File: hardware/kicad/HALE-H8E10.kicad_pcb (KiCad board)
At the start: 2 copper layers, 0 parts

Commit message: WIP checkpoint commit before spliting the 5V rail
hardware/kicad/HALE-H8E10.kicad_pcb: Manufacturing: changed the board
  outline; tenting front back → -; covering - → -; plugging - → -;
  capping - → no; filling - → no; changed the plot output settings.
  Gergő Törcsvári: updated from the schematic (added C1003, C1004,
  C2001-C2016, C3001, C3002, C21001 and 83 more, TP1001-TP1003 not
  placed yet); placed C1003, C1004, C2001-C2016, C3001, C3002, C21001
  and 82 more; routed D_CS, DS_BL, DS_RES, E_INT and 86 more nets; added
  a zone on F.Cu, B.Cu; added a zone on F.Cu, B.Cu; added a zone on
  F.Cu, B.Cu; added a zone on F.Cu, B.Cu; and 15 more changes.
hardware/kicad/HALE-H8E10.kicad_pro: Manufacturing: max arc error - →
  0.005 mm; min connection width - → 0 mm; min groove width - → 0 mm;
  min microvia diameter - → 0.2 mm; min microvia drill - → 0.1 mm; min
  resolved spokes - → 2 mm; solder mask to copper clearance - → 0 mm;
  use height for length calcs - → true mm. Gergő Törcsvári: changed the
  predefined track widths (+4); changed the predefined diff pair sizes
  (+1); changed teardrop settings; changed default text and line
  settings; changed 62 DRC rule severities; changed DRC exclusions;
  changed schematic settings; changed 19 board.design settings settings.
hardware/kicad/HALE-H8E10.kicad_sch: Gergő Törcsvári added R1002, R1003
  and TP1001-TP1003 and wired them; removed C1001, C1002, C1005, D1001
  and D1002; changed C1004 value 100nF → 10uF; changed C1004 footprint
  Capacitor_SMD:C_0603_1608Metric_Pad1.08x0.95mm_HandSolder →
  Capacitor_SMD:C_0805_2012Metric_Pad1.18x1.45mm_HandSolder; changed
  C1004 LCSC C14663 → C15850; changed C1004 wiring (pins 1 and 2 now on
  GND and +5V); changed DS1001 wiring (pin 7 now on /D_CS); and 4 more
  changes.
hardware/kicad/encoders.kicad_sch: Gergő Törcsvári changed U3001 wiring;
  changed U3002 wiring; rearranged the sheet.
hardware/kicad/keys.kicad_sch: Gergő Törcsvári added TP2001 (3V3A) and
  wired it; change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
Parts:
- added C1003: 100nF, Capacitor_SMD:C_0603_1608Metric_Pad1.08x0.95mm_HandSolder, B.Cu at (97.5, 67.5)
- added C1004: 10uF, Capacitor_SMD:C_0805_2012Metric_Pad1.18x1.45mm_HandSolder, B.Cu at (113.5, 107.0)
- added C2001: 10uF, Capacitor_SMD:C_0805_2012Metric_Pad1.18x1.45mm_HandSolder, B.Cu at (55.6, 69.8)
- added C2002: 10uF, Capacitor_SMD:C_0805_2012Metric_Pad1.18x1.45mm_HandSolder, B.Cu at (46.1, 67.5)
- added C2003: 100nF, Capacitor_SMD:C_0603_1608Metric_Pad1.08x0.95mm_HandSolder, B.Cu at (47.9, 67.8)
- added C2004: 100nF, Capacitor_SMD:C_0603_1608Metric_Pad1.08x0.95mm_HandSolder, B.Cu at (44.1, 85.6)
- added C2005: 100nF, Capacitor_SMD:C_0603_1608Metric_Pad1.08x0.95mm_HandSolder, B.Cu at (42.6, 85.6)
- added C2006: 10uF, Capacitor_SMD:C_0805_2012Metric_Pad1.18x1.45mm_HandSolder, B.Cu at (43.2, 72.5)
- added C2007: 100nF, Capacitor_SMD:C_0603_1608Metric_Pad1.08x0.95mm_HandSolder, B.Cu at (45.8, 85.6)
- added C2008: 100nF, Capacitor_SMD:C_0603_1608Metric_Pad1.08x0.95mm_HandSolder, B.Cu at (40.8, 85.6)
- added C2009: 100nF, Capacitor_SMD:C_0603_1608Metric_Pad1.08x0.95mm_HandSolder, B.Cu at (43.5, 74.2)
- added C2010: 100nF, Capacitor_SMD:C_0603_1608Metric_Pad1.08x0.95mm_HandSolder, B.Cu at (47.6, 85.6)
- added C2011: 100nF, Capacitor_SMD:C_0603_1608Metric_Pad1.08x0.95mm_HandSolder, B.Cu at (39.1, 85.6)
- added C2012: 100nF, Capacitor_SMD:C_0603_1608Metric_Pad1.08x0.95mm_HandSolder, B.Cu at (49.3, 85.6)
- added C2013: 100nF, Capacitor_SMD:C_0603_1608Metric_Pad1.08x0.95mm_HandSolder, B.Cu at (37.3, 85.6)
- added C2014: 100nF, Capacitor_SMD:C_0603_1608Metric_Pad1.08x0.95mm_HandSolder, B.Cu at (47.6, 74.6)
- added C2015: 100nF, Capacitor_SMD:C_0603_1608Metric_Pad1.08x0.95mm_HandSolder, B.Cu at (46.1, 74.6)
- added C2016: 1uF, Capacitor_SMD:C_0603_1608Metric_Pad1.08x0.95mm_HandSolder, B.Cu at (49.1, 74.6)
- added C21001: 100nF, Capacitor_SMD:C_0603_1608Metric_Pad1.08x0.95mm_HandSolder, B.Cu at (42.9, 109.3)
- added C21002: 100nF, Capacitor_SMD:C_0603_1608Metric_Pad1.08x0.95mm_HandSolder, B.Cu at (36.4, 99.7)
- added C22001: 100nF, Capacitor_SMD:C_0603_1608Metric_Pad1.08x0.95mm_HandSolder, B.Cu at (61.9, 109.3)
- added C22002: 100nF, Capacitor_SMD:C_0603_1608Metric_Pad1.08x0.95mm_HandSolder, B.Cu at (55.5, 99.7)
- added C23001: 100nF, Capacitor_SMD:C_0603_1608Metric_Pad1.08x0.95mm_HandSolder, B.Cu at (81.0, 109.3)
- added C23002: 100nF, Capacitor_SMD:C_0603_1608Metric_Pad1.08x0.95mm_HandSolder, B.Cu at (74.5, 99.7)
- added C24001: 100nF, Capacitor_SMD:C_0603_1608Metric_Pad1.08x0.95mm_HandSolder, B.Cu at (100.0, 109.3)
- added C24002: 100nF, Capacitor_SMD:C_0603_1608Metric_Pad1.08x0.95mm_HandSolder, B.Cu at (93.5, 99.7)
- added C25001: 100nF, Capacitor_SMD:C_0603_1608Metric_Pad1.08x0.95mm_HandSolder, B.Cu at (42.9, 128.3)
- added C25002: 100nF, Capacitor_SMD:C_0603_1608Metric_Pad1.08x0.95mm_HandSolder, B.Cu at (36.4, 118.7)
- added C26001: 100nF, Capacitor_SMD:C_0603_1608Metric_Pad1.08x0.95mm_HandSolder, B.Cu at (61.9, 128.3)
- added C26002: 100nF, Capacitor_SMD:C_0603_1608Metric_Pad1.08x0.95mm_HandSolder, B.Cu at (55.5, 118.7)
- added C27001: 100nF, Capacitor_SMD:C_0603_1608Metric_Pad1.08x0.95mm_HandSolder, B.Cu at (81.0, 128.3)
- added C27002: 100nF, Capacitor_SMD:C_0603_1608Metric_Pad1.08x0.95mm_HandSolder, B.Cu at (74.5, 118.7)
- added C28001: 100nF, Capacitor_SMD:C_0603_1608Metric_Pad1.08x0.95mm_HandSolder, B.Cu at (100.0, 128.3)
- added C28002: 100nF, Capacitor_SMD:C_0603_1608Metric_Pad1.08x0.95mm_HandSolder, B.Cu at (93.5, 118.7)
- added C3001: 100nF, Capacitor_SMD:C_0603_1608Metric_Pad1.08x0.95mm_HandSolder, B.Cu at (151.5, 107.2)
- added C3002: 100nF, Capacitor_SMD:C_0603_1608Metric_Pad1.08x0.95mm_HandSolder, B.Cu at (214.0, 107.2)
- added C31001: 1nF, Capacitor_SMD:C_0603_1608Metric_Pad1.08x0.95mm_HandSolder, B.Cu at (129.0, 70.3)
- added C31002: 1nF, Capacitor_SMD:C_0603_1608Metric_Pad1.08x0.95mm_HandSolder, B.Cu at (119.0, 70.3)
- added C31003: 100nF, Capacitor_SMD:C_0603_1608Metric_Pad1.08x0.95mm_HandSolder, B.Cu at (128.5, 89.0)
- added C32001: 1nF, Capacitor_SMD:C_0603_1608Metric_Pad1.08x0.95mm_HandSolder, B.Cu at (156.0, 70.3)
- added C32002: 1nF, Capacitor_SMD:C_0603_1608Metric_Pad1.08x0.95mm_HandSolder, B.Cu at (146.0, 70.3)
- added C32003: 100nF, Capacitor_SMD:C_0603_1608Metric_Pad1.08x0.95mm_HandSolder, B.Cu at (155.5, 89.0)
- added C33001: 1nF, Capacitor_SMD:C_0603_1608Metric_Pad1.08x0.95mm_HandSolder, B.Cu at (183.0, 70.3)
- added C33002: 1nF, Capacitor_SMD:C_0603_1608Metric_Pad1.08x0.95mm_HandSolder, B.Cu at (173.0, 70.3)
- added C33003: 100nF, Capacitor_SMD:C_0603_1608Metric_Pad1.08x0.95mm_HandSolder, B.Cu at (182.5, 89.0)
- added C34001: 1nF, Capacitor_SMD:C_0603_1608Metric_Pad1.08x0.95mm_HandSolder, B.Cu at (210.0, 70.3)
- added C34002: 1nF, Capacitor_SMD:C_0603_1608Metric_Pad1.08x0.95mm_HandSolder, B.Cu at (200.0, 70.3)
- added C34003: 100nF, Capacitor_SMD:C_0603_1608Metric_Pad1.08x0.95mm_HandSolder, B.Cu at (209.5, 89.0)
- added C35001: 1nF, Capacitor_SMD:C_0603_1608Metric_Pad1.08x0.95mm_HandSolder, B.Cu at (237.0, 70.3)
- added C35002: 1nF, Capacitor_SMD:C_0603_1608Metric_Pad1.08x0.95mm_HandSolder, B.Cu at (227.0, 70.3)
- added C35003: 100nF, Capacitor_SMD:C_0603_1608Metric_Pad1.08x0.95mm_HandSolder, B.Cu at (236.5, 89.0)
- added C36001: 1nF, Capacitor_SMD:C_0603_1608Metric_Pad1.08x0.95mm_HandSolder, B.Cu at (119.0, 131.8)
- added C36002: 1nF, Capacitor_SMD:C_0603_1608Metric_Pad1.08x0.95mm_HandSolder, B.Cu at (129.0, 131.8)
- added C36003: 100nF, Capacitor_SMD:C_0603_1608Metric_Pad1.08x0.95mm_HandSolder, B.Cu at (119.5, 113.1)
- added C37001: 1nF, Capacitor_SMD:C_0603_1608Metric_Pad1.08x0.95mm_HandSolder, B.Cu at (146.0, 131.8)
- added C37002: 1nF, Capacitor_SMD:C_0603_1608Metric_Pad1.08x0.95mm_HandSolder, B.Cu at (156.0, 131.8)
- added C37003: 100nF, Capacitor_SMD:C_0603_1608Metric_Pad1.08x0.95mm_HandSolder, B.Cu at (146.5, 113.1)
- added C38001: 1nF, Capacitor_SMD:C_0603_1608Metric_Pad1.08x0.95mm_HandSolder, B.Cu at (173.0, 131.8)
- added C38002: 1nF, Capacitor_SMD:C_0603_1608Metric_Pad1.08x0.95mm_HandSolder, B.Cu at (183.0, 131.8)
- added C38003: 100nF, Capacitor_SMD:C_0603_1608Metric_Pad1.08x0.95mm_HandSolder, B.Cu at (173.5, 113.1)
- added C39001: 1nF, Capacitor_SMD:C_0603_1608Metric_Pad1.08x0.95mm_HandSolder, B.Cu at (200.0, 131.8)
- added C39002: 1nF, Capacitor_SMD:C_0603_1608Metric_Pad1.08x0.95mm_HandSolder, B.Cu at (210.0, 131.8)
- added C39003: 100nF, Capacitor_SMD:C_0603_1608Metric_Pad1.08x0.95mm_HandSolder, B.Cu at (200.5, 113.1)
- added C40001: 1nF, Capacitor_SMD:C_0603_1608Metric_Pad1.08x0.95mm_HandSolder, B.Cu at (227.0, 131.8)
- added C40002: 1nF, Capacitor_SMD:C_0603_1608Metric_Pad1.08x0.95mm_HandSolder, B.Cu at (237.0, 131.8)
- added C40003: 100nF, Capacitor_SMD:C_0603_1608Metric_Pad1.08x0.95mm_HandSolder, B.Cu at (227.5, 113.1)
- added D21001: SK6812MINI-E, LED_SMD:LED_SK6812MINI-E_3.2x2.8mm_P1.5mm_ReverseMount, B.Cu at (41.0, 101.4)
- added D22001: SK6812MINI-E, LED_SMD:LED_SK6812MINI-E_3.2x2.8mm_P1.5mm_ReverseMount, B.Cu at (60.0, 101.4)
- added D23001: SK6812MINI-E, LED_SMD:LED_SK6812MINI-E_3.2x2.8mm_P1.5mm_ReverseMount, B.Cu at (79.0, 101.4)
- added D24001: SK6812MINI-E, LED_SMD:LED_SK6812MINI-E_3.2x2.8mm_P1.5mm_ReverseMount, B.Cu at (98.1, 101.4)
- added D25001: SK6812MINI-E, LED_SMD:LED_SK6812MINI-E_3.2x2.8mm_P1.5mm_ReverseMount, B.Cu at (41.0, 120.5)
- added D26001: SK6812MINI-E, LED_SMD:LED_SK6812MINI-E_3.2x2.8mm_P1.5mm_ReverseMount, B.Cu at (60.0, 120.5)
- added D27001: SK6812MINI-E, LED_SMD:LED_SK6812MINI-E_3.2x2.8mm_P1.5mm_ReverseMount, B.Cu at (79.0, 120.5)
- added D28001: SK6812MINI-E, LED_SMD:LED_SK6812MINI-E_3.2x2.8mm_P1.5mm_ReverseMount, B.Cu at (98.1, 120.5)
- added D31001: SK6812MINI-E, LED_SMD:LED_SK6812MINI-E_3.2x2.8mm_P1.5mm_ReverseMount, B.Cu at (124.0, 87.3)
- added D32001: SK6812MINI-E, LED_SMD:LED_SK6812MINI-E_3.2x2.8mm_P1.5mm_ReverseMount, B.Cu at (151.0, 87.3)
- added D33001: SK6812MINI-E, LED_SMD:LED_SK6812MINI-E_3.2x2.8mm_P1.5mm_ReverseMount, B.Cu at (178.0, 87.3)
- added D34001: SK6812MINI-E, LED_SMD:LED_SK6812MINI-E_3.2x2.8mm_P1.5mm_ReverseMount, B.Cu at (205.0, 87.3)
- added D35001: SK6812MINI-E, LED_SMD:LED_SK6812MINI-E_3.2x2.8mm_P1.5mm_ReverseMount, B.Cu at (232.0, 87.3)
- added D36001: SK6812MINI-E, LED_SMD:LED_SK6812MINI-E_3.2x2.8mm_P1.5mm_ReverseMount, B.Cu at (124.0, 114.8)
- added D37001: SK6812MINI-E, LED_SMD:LED_SK6812MINI-E_3.2x2.8mm_P1.5mm_ReverseMount, B.Cu at (151.0, 114.8)
- added D38001: SK6812MINI-E, LED_SMD:LED_SK6812MINI-E_3.2x2.8mm_P1.5mm_ReverseMount, B.Cu at (178.0, 114.8)
- added D39001: SK6812MINI-E, LED_SMD:LED_SK6812MINI-E_3.2x2.8mm_P1.5mm_ReverseMount, B.Cu at (205.0, 114.8)
- added D40001: SK6812MINI-E, LED_SMD:LED_SK6812MINI-E_3.2x2.8mm_P1.5mm_ReverseMount, B.Cu at (232.0, 114.8)
- added DS1001: Screen, HALE-git:Display_2.79_NV3007, F.Cu at (69.5, 76.8)
- added FB2001: FerriteBead, Inductor_SMD:L_0603_1608Metric_Pad1.05x0.95mm_HandSolder, B.Cu at (44.2, 69.8)
- added K21001: ks-20, HALE-git:Gateron_KS-20, F.Cu at (40.9, 106.3)
- added K22001: ks-20, HALE-git:Gateron_KS-20, F.Cu at (60.0, 106.3)
- added K23001: ks-20, HALE-git:Gateron_KS-20, F.Cu at (79.0, 106.3)
- added K24001: ks-20, HALE-git:Gateron_KS-20, F.Cu at (98.1, 106.3)
- added K25001: ks-20, HALE-git:Gateron_KS-20, F.Cu at (40.9, 125.3)
- added K26001: ks-20, HALE-git:Gateron_KS-20, F.Cu at (60.0, 125.3)
- added K27001: ks-20, HALE-git:Gateron_KS-20, F.Cu at (79.0, 125.3)
- added K28001: ks-20, HALE-git:Gateron_KS-20, F.Cu at (98.1, 125.3)
- added R1001: 220, Resistor_SMD:R_0603_1608Metric_Pad0.98x0.95mm_HandSolder, B.Cu at (98.5, 64.5)
- added R1002: 10K, Resistor_SMD:R_0603_1608Metric_Pad0.98x0.95mm_HandSolder, B.Cu at (88.2, 66.8)
- added R1003: 10K, Resistor_SMD:R_0603_1608Metric_Pad0.98x0.95mm_HandSolder, B.Cu at (69.2, 83.8)
- added R3001: 4.7K, Resistor_SMD:R_0603_1608Metric_Pad0.98x0.95mm_HandSolder, B.Cu at (88.2, 76.8)
- added R3002: 4.7K, Resistor_SMD:R_0603_1608Metric_Pad0.98x0.95mm_HandSolder, B.Cu at (88.2, 74.5)
- added R3003: 10K, Resistor_SMD:R_0603_1608Metric_Pad0.98x0.95mm_HandSolder, B.Cu at (88.2, 72.0)
- added R3004: 10K, Resistor_SMD:R_0603_1608Metric_Pad0.98x0.95mm_HandSolder, B.Cu at (90.2, 79.2)
- added RN2001: 1k, Resistor_SMD:R_Array_Convex_4x0603, B.Cu at (48.1, 90.8)
- added RN2002: 1k, Resistor_SMD:R_Array_Convex_4x0603, B.Cu at (38.6, 91.1)
- added SW31001: RotaryEncoder_Switch_MP, HALE-git:RotaryEncoder_Alps_EC12E-Switch_Vertical_H20mm, F.Cu at (124.0, 76.8)
- added SW32001: RotaryEncoder_Switch_MP, HALE-git:RotaryEncoder_Alps_EC12E-Switch_Vertical_H20mm, F.Cu at (151.0, 76.8)
- added SW33001: RotaryEncoder_Switch_MP, HALE-git:RotaryEncoder_Alps_EC12E-Switch_Vertical_H20mm, F.Cu at (178.0, 76.8)
- added SW34001: RotaryEncoder_Switch_MP, HALE-git:RotaryEncoder_Alps_EC12E-Switch_Vertical_H20mm, F.Cu at (205.0, 76.8)
- added SW35001: RotaryEncoder_Switch_MP, HALE-git:RotaryEncoder_Alps_EC12E-Switch_Vertical_H20mm, F.Cu at (232.0, 76.8)
- added SW36001: RotaryEncoder_Switch_MP, HALE-git:RotaryEncoder_Alps_EC12E-Switch_Vertical_H20mm, F.Cu at (124.0, 125.3)
- added SW37001: RotaryEncoder_Switch_MP, HALE-git:RotaryEncoder_Alps_EC12E-Switch_Vertical_H20mm, F.Cu at (151.0, 125.3)
- added SW38001: RotaryEncoder_Switch_MP, HALE-git:RotaryEncoder_Alps_EC12E-Switch_Vertical_H20mm, F.Cu at (178.0, 125.3)
- added SW39001: RotaryEncoder_Switch_MP, HALE-git:RotaryEncoder_Alps_EC12E-Switch_Vertical_H20mm, F.Cu at (205.0, 125.3)
- added SW40001: RotaryEncoder_Switch_MP, HALE-git:RotaryEncoder_Alps_EC12E-Switch_Vertical_H20mm, F.Cu at (232.0, 125.3)
- added TP1001: 5V, TestPoint:TestPoint_Pad_D2.0mm, B.Cu at (46.2, 41.8)
- added TP1002: GND, TestPoint:TestPoint_Pad_D2.0mm, B.Cu at (46.2, 45.9)
- added TP1003: 3V3, TestPoint:TestPoint_Pad_D2.0mm, B.Cu at (46.2, 49.9)
- added TP2001: 3V3A, TestPoint:TestPoint_Pad_D2.0mm, B.Cu at (38.5, 70.8)
- added U1001: 74AHCT1G125, Package_TO_SOT_SMD:SOT-23-5, B.Cu at (94.5, 65.2)
- added U1002: XIAO-ESP32-S3-Plus-SMD, HALE-git:XIAO-ESP32-S3-Plus-SMD, B.Cu at (75.0, 71.8)
- added U2001: ME6211C33M5, Package_TO_SOT_SMD:SOT-23-5, B.Cu at (50.9, 69.8)
- added U2002: MCP3208, Package_SO:SOIC-16_3.9x9.9mm_P1.27mm, B.Cu at (43.1, 80.1)
- added U21001: DRV5055A3xDBZxQ1, Package_TO_SOT_SMD:SOT-23, B.Cu at (41.0, 106.3)
- added U22001: DRV5055A3xDBZxQ1, Package_TO_SOT_SMD:SOT-23, B.Cu at (60.0, 106.3)
- added U23001: DRV5055A3xDBZxQ1, Package_TO_SOT_SMD:SOT-23, B.Cu at (79.0, 106.3)
- added U24001: DRV5055A3xDBZxQ1, Package_TO_SOT_SMD:SOT-23, B.Cu at (98.1, 106.3)
- added U25001: DRV5055A3xDBZxQ1, Package_TO_SOT_SMD:SOT-23, B.Cu at (41.0, 125.3)
- added U26001: DRV5055A3xDBZxQ1, Package_TO_SOT_SMD:SOT-23, B.Cu at (60.0, 125.3)
- added U27001: DRV5055A3xDBZxQ1, Package_TO_SOT_SMD:SOT-23, B.Cu at (79.0, 125.3)
- added U28001: DRV5055A3xDBZxQ1, Package_TO_SOT_SMD:SOT-23, B.Cu at (98.1, 125.3)
- added U3001: MCP23017x-x-SS, Package_SO:SSOP-28_5.3x10.2mm_P0.65mm, B.Cu at (153.8, 101.8)
- added U3002: MCP23017x-x-SS, Package_SO:SSOP-28_5.3x10.2mm_P0.65mm, B.Cu at (216.0, 101.8)
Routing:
- net +5V: track 0.00 -> 653.2 mm, vias 0 -> 30
- net +3.3V: track 0.00 -> 195.5 mm, vias 0 -> 8
- net /encoders/I2C_SDA: track 0.00 -> 148.3 mm, vias 0 -> 2
- net /E_INT: track 0.00 -> 141.5 mm, vias 0 -> 3
- net /encoders/I2C_SCL: track 0.00 -> 130.5 mm, vias 0 -> 2
- net /encoders/RESET: track 0.00 -> 117.9 mm, vias 0 -> 2
- net /keys/H4: track 0.00 -> 106.8 mm
- net /keys/LED_L1_OUT: track 0.00 -> 106.4 mm, vias 0 -> 3
- net /keys/H8: track 0.00 -> 105.7 mm
- net GND: track 0.00 -> 97.8 mm, vias 0 -> 47
- net /keys/H3: track 0.00 -> 87.2 mm
- net /keys/H7: track 0.00 -> 85.2 mm
- net /encoders/ENC_B6: track 0.00 -> 81.9 mm
- net /encoders/ENC_B3: track 0.00 -> 74.0 mm
- net /E6_SW: track 0.00 -> 71.2 mm, vias 0 -> 2
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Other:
- board outline added: 217 x 77.7 mm

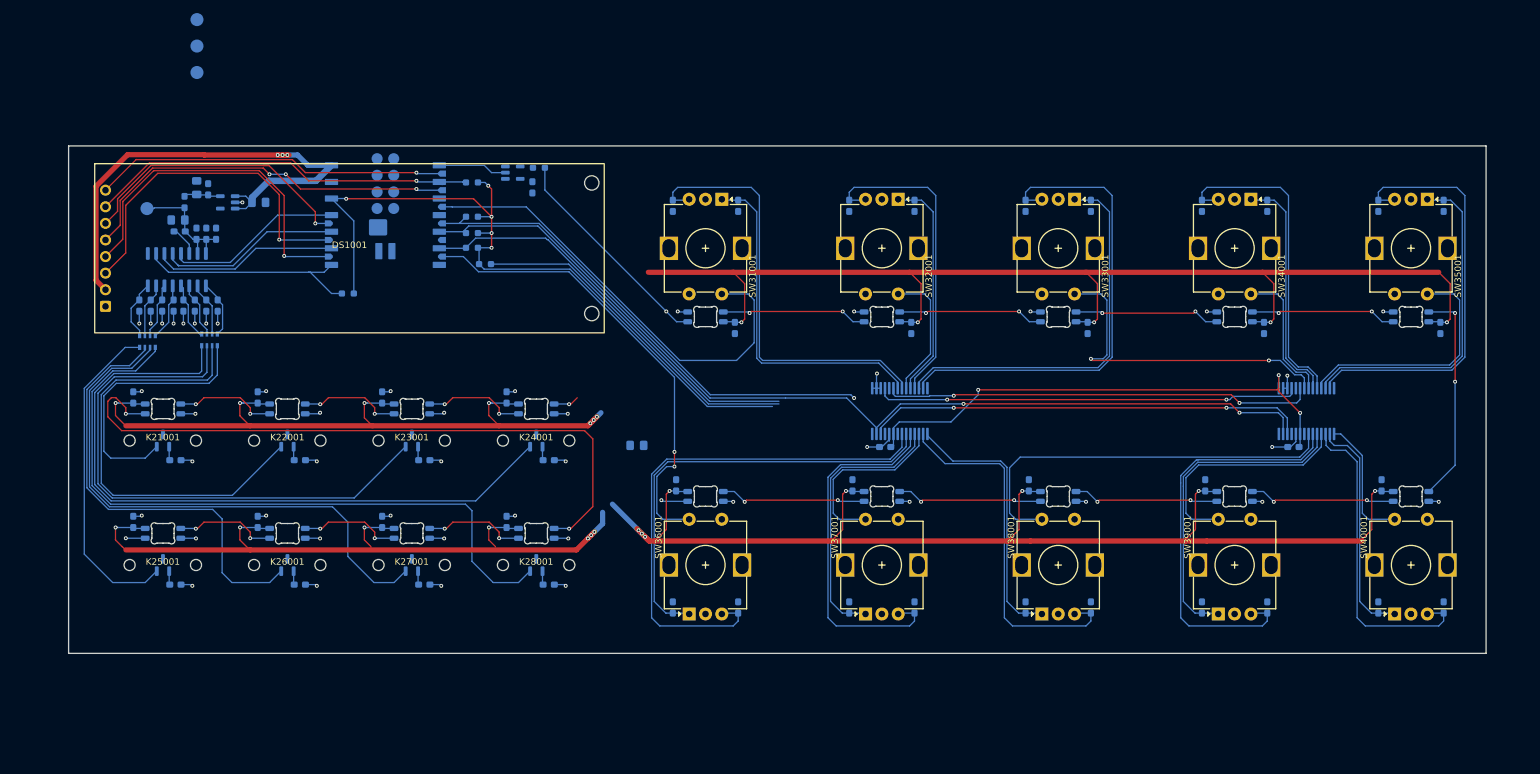
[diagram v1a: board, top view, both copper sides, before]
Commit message: "finished" PCB
hardware/kicad/HALE-H8E10.kicad_pcb: Manufacturing: changed the board
  outline. Gergő Törcsvári: updated from the schematic (added C1001,
  C1002, C1004-C1009, H1001-H1012, R1004, R1005 and 5 more; removed
  R1002 and R1003; nets changed on 44 pads); placed C1001, C1002,
  C1004-C1009, H1001-H1012, R1004, R1005 and 4 more; added REF**;
  removed C1004; moved C1003, C2002, C2003, C2006, R1001, TP2001 and
  U1001; routed EN_AUX, EN_LED, +5V_AUX, +5V_LED and 3 more nets;
  rerouted D_CS, DS_BL, DS_RES, E_INT and 21 more nets; and 3 more
  changes.
hardware/kicad/HALE-H8E10.kicad_pro: Gergő Törcsvári excluded 2 DRC
  violations; changed schematic settings.
hardware/kicad/HALE-H8E10.kicad_sch: Gergő Törcsvári added C1001, C1002,
  C1005-C1009, H1001-H1012, R1004, R1005 and 4 more and wired them;
  removed R1002 and R1003; changed 4 parts' fields; changed C1004 wiring
  (pin 1 now on +5V); renamed net unconnected-(U1002-D3-Pad4) to
  /EN_AUX; renamed net unconnected-(U1002-D15-Pad19) to /EN_LED; split
  +5V into +5V_AUX and +5V_LED; and 4 more changes.
hardware/kicad/encoder.kicad_sch: Gergő Törcsvári changed 10 parts'
  fields; renamed net unconnected-(U1002-D3-Pad4) to /EN_AUX; renamed
  net unconnected-(U1002-D15-Pad19) to /EN_LED; split +5V into +5V_AUX
  and +5V_LED.
hardware/kicad/encoders.kicad_sch: Gergő Törcsvári changed 6 parts'
  fields; renamed net unconnected-(U1002-D3-Pad4) to /EN_AUX; renamed
  net unconnected-(U1002-D15-Pad19) to /EN_LED; split +5V into +5V_AUX
  and +5V_LED.
hardware/kicad/key_cell.kicad_sch: Gergő Törcsvári changed 16 parts'
  fields; renamed net unconnected-(U1002-D3-Pad4) to /EN_AUX; renamed
  net unconnected-(U1002-D15-Pad19) to /EN_LED; split +5V into +5V_AUX
  and +5V_LED.
hardware/kicad/keys.kicad_sch: Gergő Törcsvári added R2001 (10K) and
  wired it to /KEYS_CS; changed 6 parts' fields; renamed net
  unconnected-(U1002-D3-Pad4) to /EN_AUX; renamed net
  unconnected-(U1002-D15-Pad19) to /EN_LED; split +5V into +5V_A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
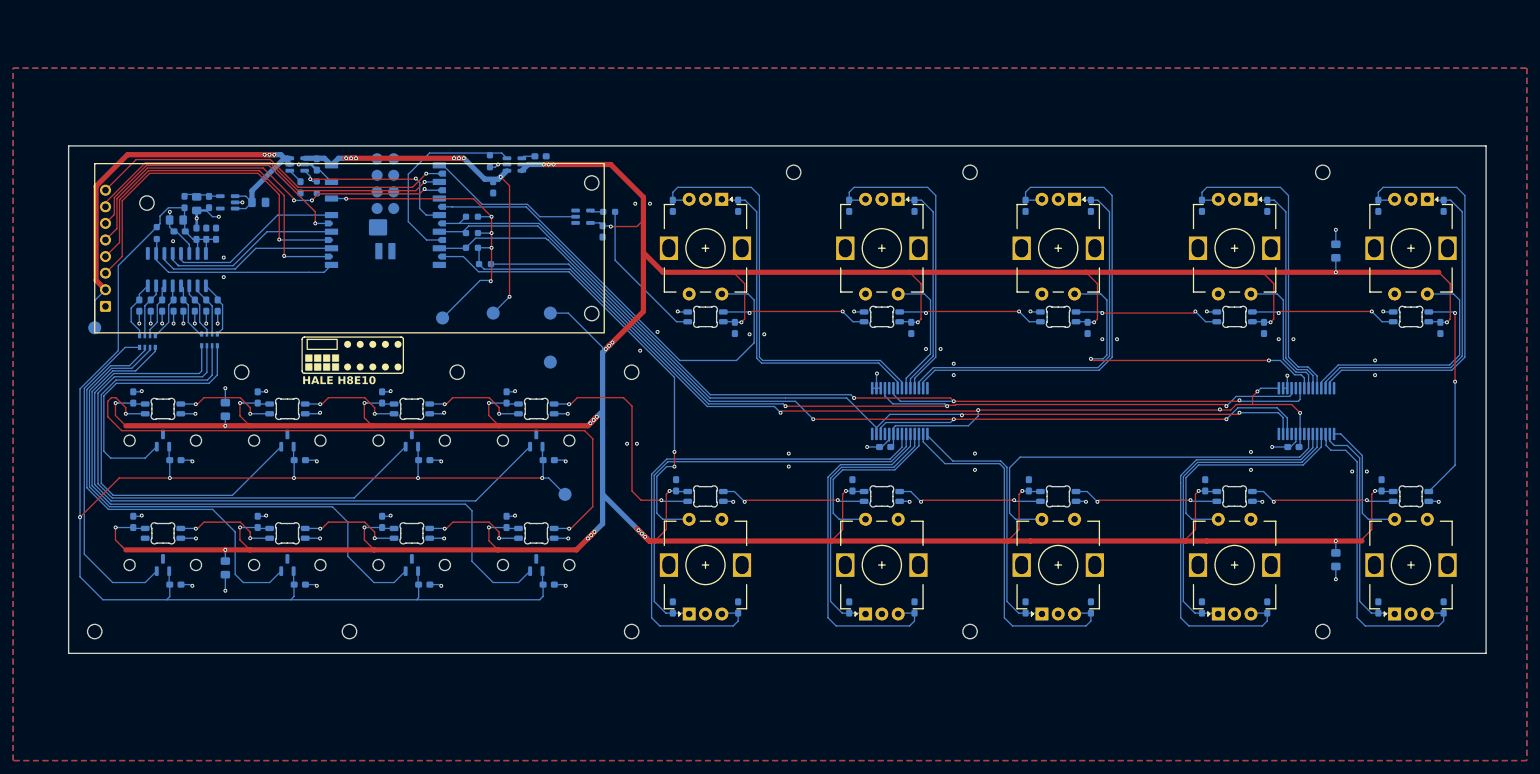
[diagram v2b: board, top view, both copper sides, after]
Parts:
- removed R1002, R1003: 10K, Resistor_SMD:R_0603_1608Metric_Pad0.98x0.95mm_HandSolder
- added C1001: 100nF, Capacitor_SMD:C_0603_1608Metric_Pad1.08x0.95mm_HandSolder, B.Cu at (62.0, 67.5)
- added C1002: 100nF, Capacitor_SMD:C_0603_1608Metric_Pad1.08x0.95mm_HandSolder, B.Cu at (98.8, 62.8)
- added C1005: 1uF, Capacitor_SMD:C_0603_1608Metric_Pad1.08x0.95mm_HandSolder, B.Cu at (64.5, 64.0)
- added C1006: 10uF, Capacitor_SMD:C_0805_2012Metric_Pad1.18x1.45mm_HandSolder, B.Cu at (50.5, 101.5)
- added C1007: 10uF, Capacitor_SMD:C_0805_2012Metric_Pad1.18x1.45mm_HandSolder, B.Cu at (50.5, 125.8)
- added C1008: 10uF, Capacitor_SMD:C_0805_2012Metric_Pad1.18x1.45mm_HandSolder, B.Cu at (220.5, 77.2)
- added C1009: 10uF, Capacitor_SMD:C_0805_2012Metric_Pad1.18x1.45mm_HandSolder, B.Cu at (220.5, 124.5)
- added H1001: MountingHole, MountingHole:MountingHole_2.2mm_M2, F.Cu at (30.5, 135.5)
- added H1002: MountingHole, MountingHole:MountingHole_2.2mm_M2, F.Cu at (69.5, 135.5)
- added H1003: MountingHole, MountingHole:MountingHole_2.2mm_M2, F.Cu at (112.7, 135.5)
- added H1004: MountingHole, MountingHole:MountingHole_2.2mm_M2, F.Cu at (53.0, 95.8)
- added H1005: MountingHole, MountingHole:MountingHole_2.2mm_M2, F.Cu at (86.0, 95.8)
- added H1006: MountingHole, MountingHole:MountingHole_2.2mm_M2, F.Cu at (112.7, 95.8)
- added H1007: MountingHole, MountingHole:MountingHole_2.2mm_M2, F.Cu at (137.5, 65.2)
- added H1008: MountingHole, MountingHole:MountingHole_2.2mm_M2, F.Cu at (164.5, 135.5)
- added H1009: MountingHole, MountingHole:MountingHole_2.2mm_M2, F.Cu at (164.5, 65.2)
- added H1010: MountingHole, MountingHole:MountingHole_2.2mm_M2, F.Cu at (218.5, 65.2)
- added H1011: MountingHole, MountingHole:MountingHole_2.2mm_M2, F.Cu at (218.5, 135.5)
- added H1012: MountingHole, MountingHole:MountingHole_2.2mm_M2, F.Cu at (38.5, 69.9)
- added R1004: 10K, Resistor_SMD:R_0603_1608Metric_Pad0.98x0.95mm_HandSolder, B.Cu at (91.0, 63.5)
- added R1005: 10K, Resistor_SMD:R_0603_1608Metric_Pad0.98x0.95mm_HandSolder, B.Cu at (64.5, 67.5)
- added R2001: 10K, Resistor_SMD:R_0603_1608Metric_Pad0.98x0.95mm_HandSolder, B.Cu at (40.0, 74.5)
- added REF**: Logo H8E10, HALE-git:Logo H8E10, B.Cu at (69.5, 93.5)
- added REF**: Logo H8E10, HALE-git:Logo H8E10, F.Cu at (70.5, 93.5)
- added TP1004: 5V_LED, TestPoint:TestPoint_Pad_D2.0mm, B.Cu at (100.2, 86.8)
- added TP1005: 5V_AUX, TestPoint:TestPoint_Pad_D2.0mm, B.Cu at (30.5, 89.0)
- added U1003: TPS22810DBV, Package_TO_SOT_SMD:SOT-23-6, B.Cu at (61.5, 64.0)
- added U1004: TPS22810DBV, Package_TO_SOT_SMD:SOT-23-6, B.Cu at (94.8, 64.0)
- C1004: value 10uF -> 1uF; footprint Capacitor_SMD:C_0805_2012Metric_Pad1.18x1.45mm_HandSolder -> Capacitor_SMD:C_0603_1608Metric_Pad1.08x0.95mm_HandSolder
- moved TP2001 77.5 mm to (102.5, 114.5)
- moved TP1002 72.6 mm to (100.2, 94.2)
- moved TP1001 63.8 mm to (91.5, 86.8)
- moved TP1003 53.2 mm to (83.8, 87.5)
- moved C1004 45.2 mm to (91.5, 67.5), turned to -90 degrees
- moved C1003 12.7 mm to (108.2, 74.2)
- moved R1001 12.7 mm to (109.2, 71.2)
- moved U1001 12.7 mm to (105.2, 72.0)
- moved C2002 2.45 mm to (46.1, 70.0), turned to -90 degrees
- moved C2003 1.95 mm to (48.0, 69.8), turned to -90 degrees
- moved C2006 0.25 mm to (43.0, 72.5)
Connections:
- C1003 pad 2: +5V -> +5V_LED
- C1004 pad 1: GND -> +5V
- C1004 pad 2: +5V -> GND
- C2001 pad 1: +5V -> +5V_AUX
- C21002 pad 1: +5V -> +5V_LED
- C22002 pad 1: +5V -> +5V_LED
- C23002 pad 1: +5V -> +5V_LED
- C24002 pad 1: +5V -> +5V_LED
- C25002 pad 1: +5V -> +5V_LED
- C26002 pad 1: +5V -> +5V_LED
- C27002 pad 1: +5V -> +5V_LED
- C28002 pad 1: +5V -> +5V_LED
- C31003 pad 1: +5V -> +5V_LED
- C32003 pad 1: +5V -> +5V_LED
- C33003 pad 1: +5V -> +5V_LED
- C34003 pad 1: +5V -> +5V_LED
- C35003 pad 1: +5V -> +5V_LED
- C36003 pad 1: +5V -> +5V_LED
- C37003 pad 1: +5V -> +5V_LED
- C38003 pad 1: +5V -> +5V_LED
- C39003 pad 1: +5V -> +5V_LED
- C40003 pad 1: +5V -> +5V_LED
- D21001 pad 3: +5V -> +5V_LED
- D22001 pad 3: +5V -> +5V_LED
- D23001 pad 3: +5V -> +5V_LED
- D24001 pad 3: +5V -> +5V_LED
- D25001 pad 3: +5V -> +5V_LED
- D26001 pad 3: +5V -> +5V_LED
- D27001 pad 3: +5V -> +5V_LED
- D28001 pad 3: +5V -> +5V_LED
- D31001 pad 3: +5V -> +5V_LED
- D32001 pad 3: +5V -> +5V_LED
- D33001 pad 3: +5V -> +5V_LED
- D34001 pad 3: +5V -> +5V_LED
- D35001 pad 3: +5V -> +5V_LED
- D36001 pad 3: +5V -> +5V_LED
- D37001 pad 3: +5V -> +5V_LED
- D38001 pad 3: +5V -> +5V_LED
- D39001 pad 3: +5V -> +5V_LED
- D40001 pad 3: +5V -> +5V_LED
- DS1001 pad 2: +5V -> +5V_AUX
- U1001 pad 5: +5V -> +5V_LED
- U1002 pad 19: unconnected-(U1002-D15-Pad19) -> /EN_LED
- U1002 pad 4: unconnected-(U1002-D3-Pad4) -> /EN_AUX
- U2001 pad 1: +5V -> +5V_AUX
- U2001 pad 3: +5V -> +5V_AUX
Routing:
- net +5V_LED: track 0.00 -> 682.6 mm, vias 0 -> 38
- net +5V: track 653.2 -> 60.1 mm, vias 30 -> 8
- net +3.3VA: track 35.9 -> 265.4 mm, vias 0 -> 5
- net +5V_AUX: track 0.00 -> 72.2 mm, vias 0 -> 3
- net /encoders/LED_L1_IN: track 36.6 -> 0.00 mm, vias 1 -> 0
- net /KEYS_LED_DATA_IN: track 0.00 -> 35.1 mm
- net /EN_LED: track 0.00 -> 30.4 mm
- net /encoders/I2C_SCL: track 130.5 -> 158.4 mm, vias 2 -> 3
- net /EN_AUX: track 0.00 -> 27.3 mm, vias 0 -> 2
- net GND: track 97.8 -> 124.6 mm, vias 47 -> 85
- net /encoders/RESET: track 117.9 -> 144.6 mm, vias 2 -> 3
- net +3.3V: track 195.5 -> 219.8 mm, vias 8 -> 10
- net /E_LED_DATA_IN: track 0.00 -> 22.4 mm, vias 1 -> 0
- net /E_INT: track 141.5 -> 156.7 mm
- net /LED_DATA: track 10.6 -> 24.1 mm
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- added copper zone on B.Cu, net GND
- added copper zone on F.Cu, net GND
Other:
- board text added: "Rev 1.0 - 2026.10.19."
